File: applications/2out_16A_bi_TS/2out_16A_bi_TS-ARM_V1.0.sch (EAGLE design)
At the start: 31 parts, among them K1 HFE20-1/024-1HD-L2, K2 HFE20-1/024-1HD-L2, T1 BC847, T2 BC847, T3 BC847, T4 BC847

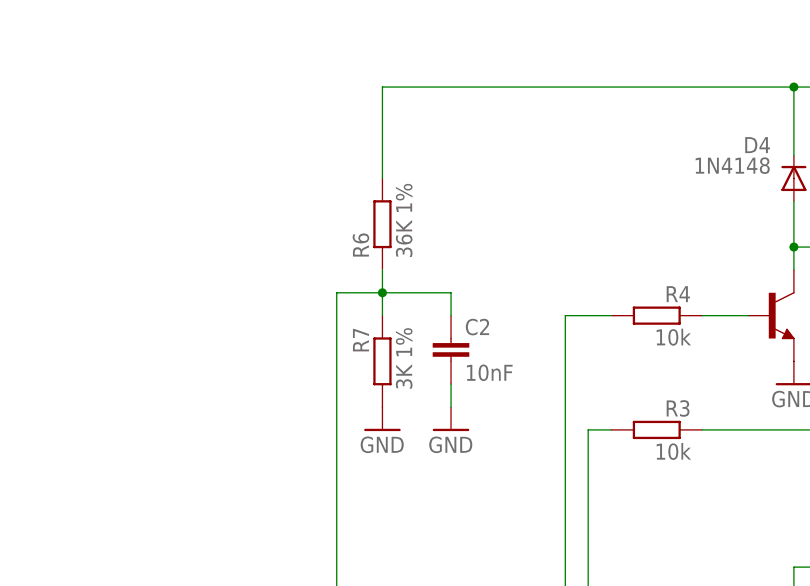
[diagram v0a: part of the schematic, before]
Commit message: Spannungsteiler auf 91k/10k geändert
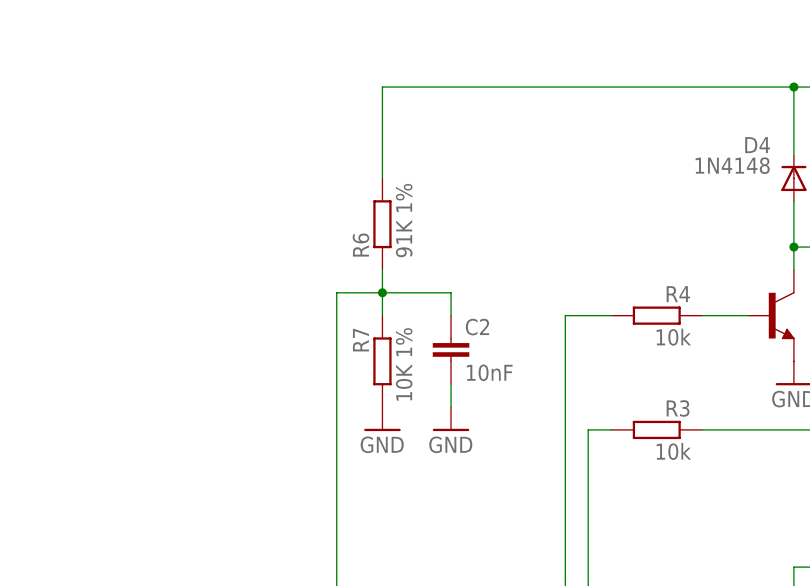
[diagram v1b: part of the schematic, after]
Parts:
- R6: value 36K 1% -> 91K 1%
- R7: value 3K 1% -> 10K 1%
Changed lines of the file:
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@@
 <part name="K2" library="meine_lib" deviceset="RT?F*" device="314" technology="24" value="HFE20-1/024-1HD-L2"/>
 <part name="JP1" library="pinhead" deviceset="PINHD-1X8" device=""/>
-<part name="R6" library="rcl" deviceset="R-EU_" device="M1206" value="36K 1%"/>
-<part name="R7" library="rcl" deviceset="R-EU_" device="M1206" value="3K 1%"/>
+<part name="R6" library="rcl" deviceset="R-EU_" device="M1206" value="91K 1%"/>
+<part name="R7" library="rcl" deviceset="R-EU_" device="M1206" value="10K 1%"/>
 <part name="C2" library="rcl" deviceset="C-EU" device="C1206K" value="10nF"/>
 <part name="GND5" library="supply1" deviceset="GND" device=""/>
